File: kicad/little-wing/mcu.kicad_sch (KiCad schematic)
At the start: 31 parts, among them SW2 Reset, U1 ${ALTIUM_VALUE}, X1 ${ALTIUM_VALUE}, X2 ${ALTIUM_VALUE}

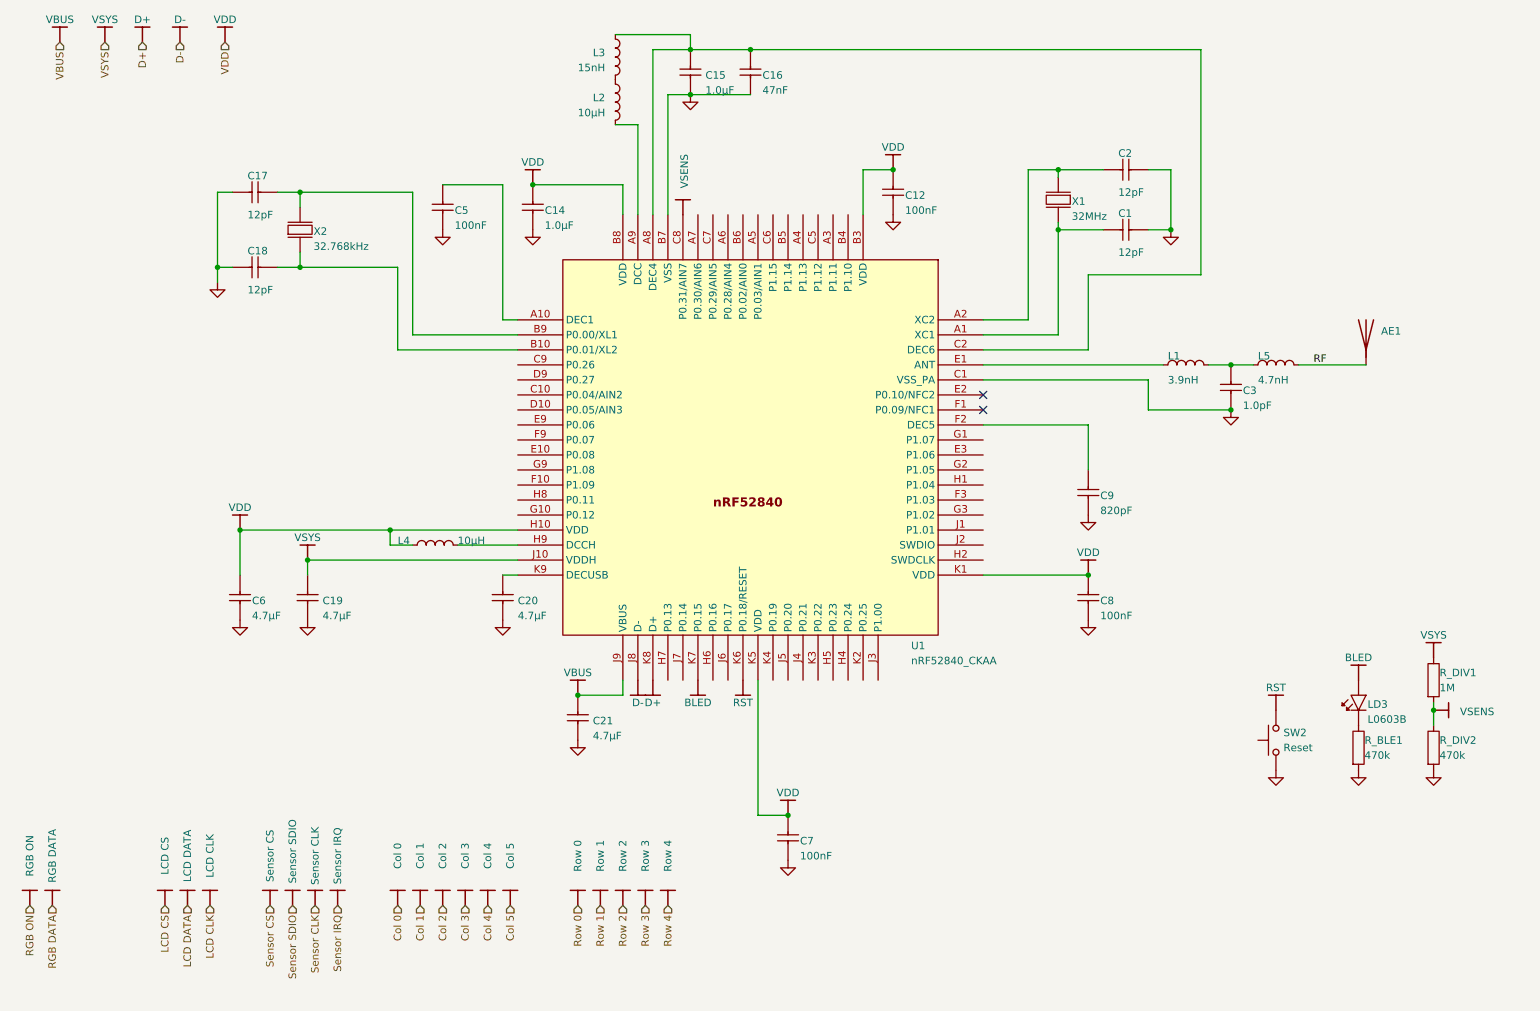
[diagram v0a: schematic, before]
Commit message: Reseting all the extra components sizes
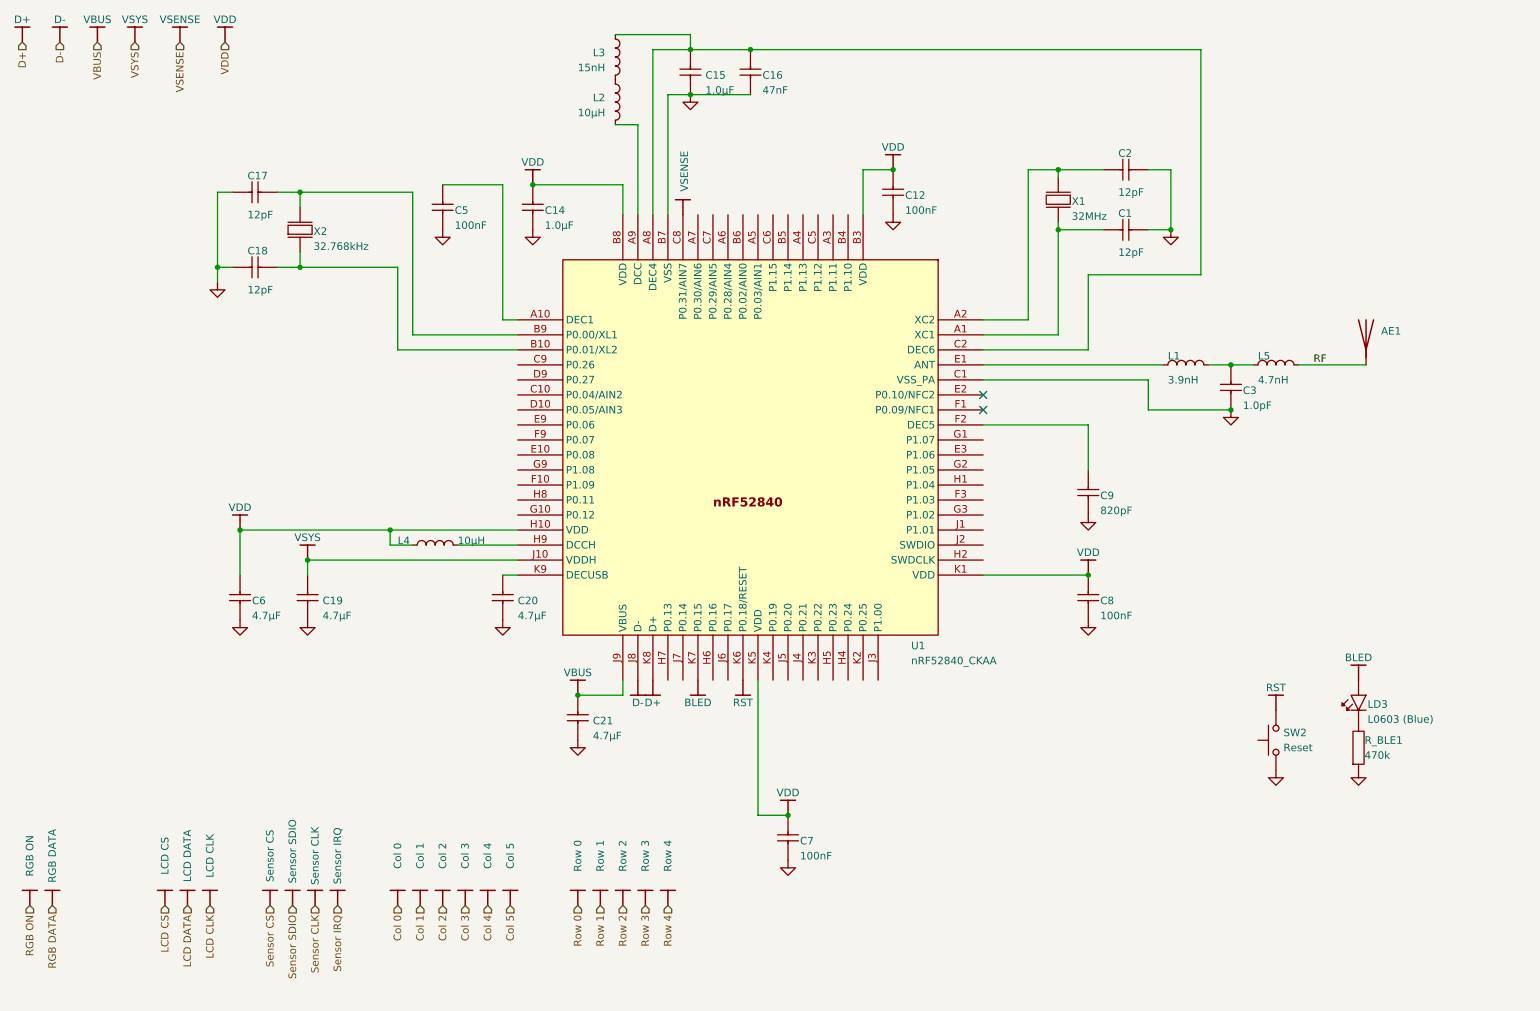
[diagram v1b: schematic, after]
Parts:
- removed R_DIV1: 1M, RESC0603X03L_C, symbol AltiumLib:root_3_mirrored_RES_AltiumLib.DbLib
- removed R_DIV2: 470k, RESC0603X03L_C, symbol AltiumLib:root_3_mirrored_RES_AltiumLib.DbLib
- LD3: value L0603B -> L0603 (Blue); footprint LED_0603_R -> LED_SMD:LED_0201_0603Metric
- R_BLE1: footprint RESC0603X03L_C -> Resistor_SMD:R_0201_0603Metric
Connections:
- net VSENS renamed VSENSE

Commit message: Swapping the crystals for smaller ones
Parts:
- X1: footprint BT-XTAL_2016 -> Crystal:Crystal_SMD_1210-4Pin_1.2x1.0mm
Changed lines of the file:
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@@
 			)
 		)
-		(property "Footprint" "BT-XTAL_2016"
+		(property "Footprint" "Crystal:Crystal_SMD_1210-4Pin_1.2x1.0mm"
 			(at 198.12 57.15 0)
 			(effects

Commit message: Dialing in the physical package
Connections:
- no-connect marks 2 -> 5
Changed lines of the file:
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@@
+	)
+	(no_connect
+		(at 154.94 55.88)
+	)
+	(no_connect
+		(at 160.02 55.88)
 	)
 	(no_connect
@@
 		(at 185.42 88.9)
 	)
+	(no_connect
+		(at 147.32 55.88)
+	)
 	(wire

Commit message: Backporting footprints from the PCB back to schematic
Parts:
- AE1: footprint JTI Antenna:ANTC3216X140N -> YAGEO Antenna:ANT2012LL13R2400A
- C1, C17, C18, C2, C3, C5, C7, C8, C9: footprint CAPC0603X03L_C -> Capacitor_SMD:C_0201_0603Metric
- C12, C16: footprint CAPC0603X03L_C -> Passive:CAPC0603X03L_C
- C14, C15, C19, C20, C21, C6: footprint CAPC1608X06L -> Passive:CAPC1608X06L
- L1: footprint INDC0603X03L_C -> Inductors$:INDC0603X03L_C
- L2: footprint INDC1608X06L -> 0603:INDC1608X06L
- L3: footprint INDC1005X04L -> 0402:INDC1005X04L
- L4: footprint INDC1608X06L -> Passive:INDC1608X06L
- L5: footprint INDC0603X03L_C -> Passive:INDC0603X03L_C
- SW2: footprint Button_Switch_SMD:SW_SPST_B3U-1000P -> Button_Switch_SMD:SW_SPST_B3U-3000P
- U1: footprint BGA94C35P10X10_352X356X50 -> nRF Devices$:BGA94C35P10X10_352X356X50
- X2: footprint XTAL_2012 -> EXC-1210:XTAL_ECS32761210TR
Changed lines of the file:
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@@
 			)
 		)
-		(property "Footprint" "BGA94C35P10X10_352X356X50"
+		(property "Footprint" "nRF Devices$:BGA94C35P10X10_352X356X50"
 			(at 114.3 127 0)
 			(effects
@@
 			)
 		)
-		(property "Footprint" "CAPC0603X03L_C"
+		(property "Footprint" "Capacitor_SMD:C_0201_0603Metric"
 			(at 205.74 58.42 0)
 			(effects
@@
 			)
 		)
-		(property "Footprint" "CAPC1608X06L"
+		(property "Footprint" "Passive:CAPC1608X06L"
 			(at 135.89 35.56 0)
 			(effects
@@
 			)
 		)
-		(property "Footprint" "Button_Switch_SMD:SW_SPST_B3U-1000P"
+		(property "Footprint" "Button_Switch_SMD:SW_SPST_B3U-3000P"
 			(at 229.87 144.78 0)
 			(effects
@@
 			)
 		)
-		(property "Footprint" "CAPC0603X03L_C"
+		(property "Footprint" "Passive:CAPC0603X03L_C"
 			(at 146.05 27.94 0)
 			(effects
@@
 			)
 		)
-		(property "Footprint" "CAPC0603X03L_C"
+		(property "Footprint" "Capacitor_SMD:C_0201_0603Metric"
 			(at 227.33 88.9 0)
 			(effects
@@
 			)
 		)
-		(property "Footprint" "INDC1608X06L"
+		(property "Footprint" "Passive:INDC1608X06L"
 			(at 88.9 111.76 0)
 			(effects
@@
 			)
 		)
-		(property "Footprint" "CAPC1608X06L"
+		(property "Footprint" "Passive:CAPC1608X06L"
 			(at 104.14 116.84 0)
 			(effects
@@
 			)
 		)
-		(property "Footprint" "CAPC0603X03L_C"
+		(property "Footprint" "Capacitor_SMD:C_0201_0603Metric"
 			(at 205.74 48.26 0)
 			(effects
@@
 			)
 		)
-		(property "Footprint" "INDC0603X03L_C"
+		(property "Footprint" "Passive:INDC0603X03L_C"
 			(at 231.14 81.28 0)
 			(effects
@@
 			)
 		)
-		(property "Footprint" "CAPC0603X03L_C"
+		(property "Footprint" "Capacitor_SMD:C_0201_0603Metric"
 			(at 66.04 52.07 0)
 			(effects
@@
 			)
 		)
-		(property "Footprint" "CAPC0603X03L_C"
+		(property "Footprint" "Capacitor_SMD:C_0201_0603Metric"
 			(at 152.4 157.48 0)
 			(effects
@@
 			)
 		)
-		(property "Footprint" "CAPC1608X06L"
+		(property "Footprint" "Passive:CAPC1608X06L"
 			(at 59.69 116.84 0)
 			(effects
@@
 			)
 		)
-		(property "Footprint" "CAPC0603X03L_C"
+		(property "Footprint" "Passive:CAPC0603X03L_C"
 			(at 170.18 48.26 0)
 			(effects
@@
 			)
 		)
-		(property "Footprint" "CAPC1608X06L"
+		(property "Footprint" "Passive:CAPC1608X06L"
 			(at 109.22 50.8 0)
 			(effects
@@
 			)
 		)
-		(property "Footprint" "CAPC0603X03L_C"
+		(property "Footprint" "Capacitor_SMD:C_0201_0603Metric"
 			(at 203.2 116.84 0)
 			(effects
@@
 			)
 		)
-		(property "Footprint" "JTI Antenna:ANTC3216X140N"
+		(property "Footprint" "YAGEO Antenna:ANT2012LL13R2400A"
 			(at 250.19 76.2 0)
 			(effects
@@
 			)
 		)
-		(property "Footprint" "INDC1005X04L"
+		(property "Footprint" "0402:INDC1005X04L"
 			(at 123.19 25.4 0)
 			(effects
@@
 			)
 		)
-		(property "Footprint" "CAPC1608X06L"
+		(property "Footprint" "Passive:CAPC1608X06L"
 			(at 71.12 116.84 0)
 			(effects
@@
 			)
 		)
-		(property "Footprint" "CAPC0603X03L_C"
+		(property "Footprint" "Capacitor_SMD:C_0201_0603Metric"
 			(at 66.04 64.77 0)
 			(effects
@@
 			)
 		)
-		(property "Footprint" "CAPC0603X03L_C"
+		(property "Footprint" "Capacitor_SMD:C_0201_0603Metric"
 			(at 203.2 99.06 0)
 			(effects
@@
 			)
 		)
-		(property "Footprint" "CAPC1608X06L"
+		(property "Footprint" "Passive:CAPC1608X06L"
 			(at 116.84 137.16 0)
 			(effects
@@
 			)
 		)
-		(property "Footprint" "CAPC0603X03L_C"
+		(property "Footprint" "Capacitor_SMD:C_0201_0603Metric"
 			(at 93.98 50.8 0)
 			(effects
@@
 			)
 		)
-		(property "Footprint" "INDC0603X03L_C"
+		(property "Footprint" "Inductors$:INDC0603X03L_C"
 			(at 215.9 81.28 0)
 			(effects
@@
 			)
 		)
-		(property "Footprint" "INDC1608X06L"
+		(property "Footprint" "0603:INDC1608X06L"
 			(at 123.19 33.02 0)
 			(effects
@@
 			)
 		)
-		(property "Footprint" "XTAL_2012"
+		(property "Footprint" "EXC-1210:XTAL_ECS32761210TR"
 			(at 69.85 54.61 0)
 			(effects

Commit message: Fixes and space optimisations
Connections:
- net BLED: now also U1.G10 (P0.12); no longer U1.K7 (P0.15)
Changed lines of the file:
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@@
 	)
 	(symbol
-		(lib_id "nrf52840_ckaa_var4-altium-import:VDD_nRF_BAR")
-		(at 137.16 134.62 0)
-		(unit 1)
-		(exclude_from_sim no)
-		(in_bom yes)
-		(on_board yes)
-		(dnp no)
-		(property "Reference" "#PWR0109"
-			(at 137.16 134.62 0)
-			(effects
-				(font
-					(size 1.27 1.27)
-				)
-				(hide yes)
-			)
-		)
-		(property "Value" "BLED"
-			(at 137.16 138.43 0)
-			(effects
-				(font
-					(size 1.27 1.27)
-				)
-			)
-		)
-		(property "Footprint" ""
-			(at 137.16 134.62 0)
-			(effects
-				(font
-					(size 1.27 1.27)
-				)
-			)
-		)
-		(property "Datasheet" ""
-			(at 137.16 134.62 0)
-			(effects
-				(font
-					(size 1.27 1.27)
-				)
-			)
-		)
-		(property "Description" ""
-			(at 137.16 134.62 0)
-			(effects
-				(font
-					(size 1.27 1.27)
-				)
-			)
-		)
-		(pin ""
-		)
-		(instances
-			(project "little-wing"
-				(path "/3a835e6f-a660-4b38-a102-87841cdd95ed/eaaf4618-ba3d-41b4-8a99-4f719e243661/ebcf195d-f1fd-431a-a78e-86a1a85cb647"
-					(reference "#PWR0109")
-					(unit 1)
-				)
-			)
-		)
-	)
-	(symbol
 		(lib_id "npm1100_caax_config1-altium-import:VBUS_BAR")
 		(at 90.17 172.72 180)
@@
 					(unit 1)
 				)
+			)
+		)
+	)
+	(symbol
+		(lib_id "nrf52840_ckaa_var4-altium-import:VDD_nRF_BAR")
+		(at 106.68 106.68 270)
+		(unit 1)
+		(exclude_from_sim no)
+		(in_bom yes)
+		(on_board yes)
+		(dnp no)
+		(property "Reference" "#PWR064"
+			(at 106.68 106.68 0)
+			(effects
+				(font
+					(size 1.27 1.27)
+				)
+				(hide yes)
+			)
+		)
+		(property "Value" "BLED"
+			(at 102.87 106.68 0)
+			(effects
+				(font
+					(size 1.27 1.27)
+				)
+			)
+		)
+		(property "Footprint" ""
+			(at 106.68 106.68 0)
+			(effects
+				(font
+					(size 1.27 1.27)
+				)
+			)
+		)
+		(property "Datasheet" ""
+			(at 106.68 106.68 0)
+			(effects
+				(font
+					(size 1.27 1.27)
+				)
+			)
+		)
+		(property "Description" ""
+			(at 106.68 106.68 0)
+			(effects
+				(font
+					(size 1.27 1.27)
+				)
+			)
+		)
+		(pin ""
+		)
+		(instances
+			(project "little-wing"
+				(path "/3a835e6f-a660-4b38-a102-87841cdd95ed/eaaf4618-ba3d-41b4-8a99-4f719e243661/ebcf195d-f1fd-431a-a78e-86a1a85cb647"
+					(reference "#PWR064")
+					(unit 1)
+				)

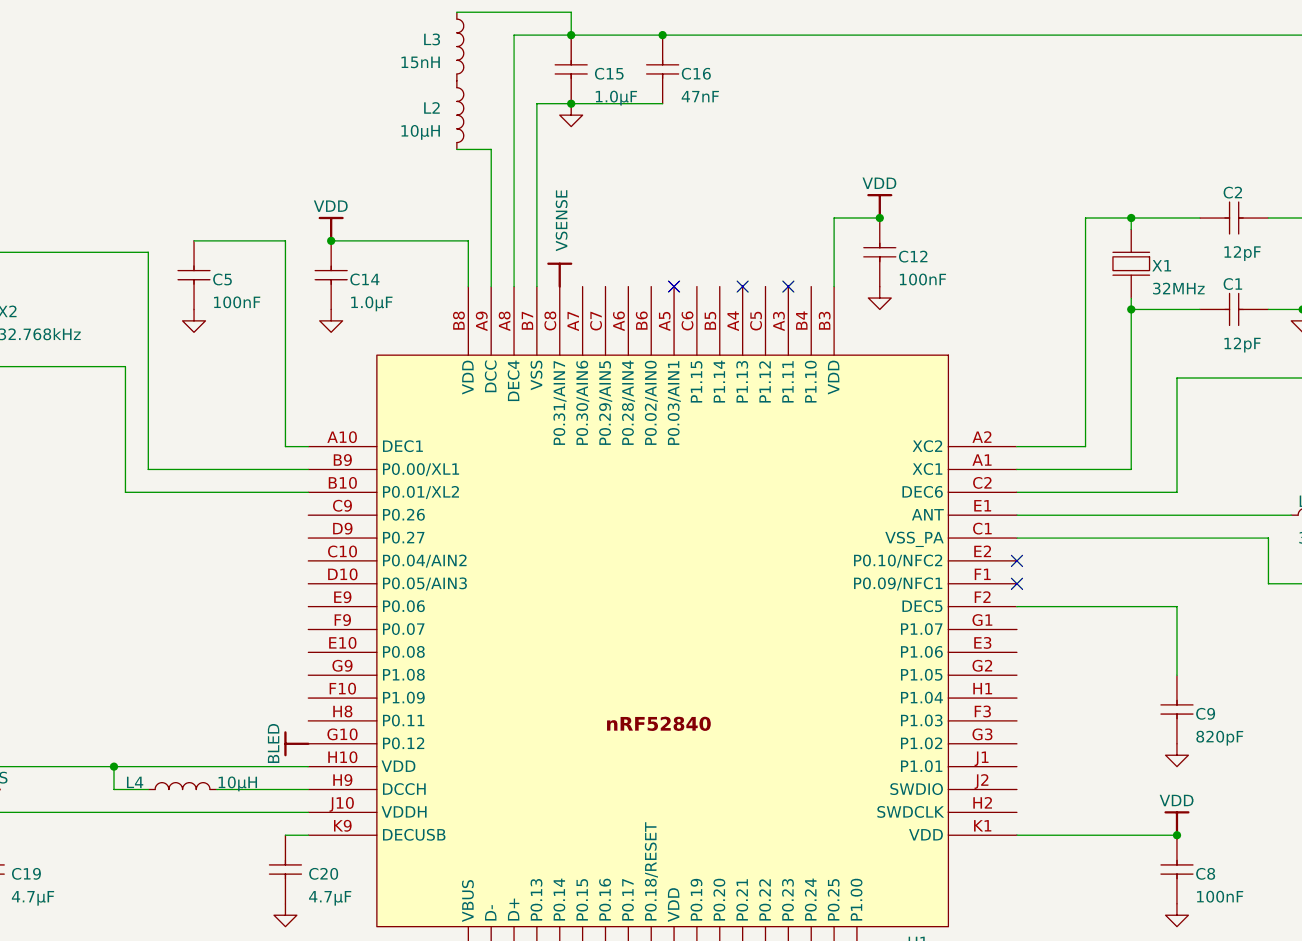
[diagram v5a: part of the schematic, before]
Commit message: Loosely attaching pins to prefiery
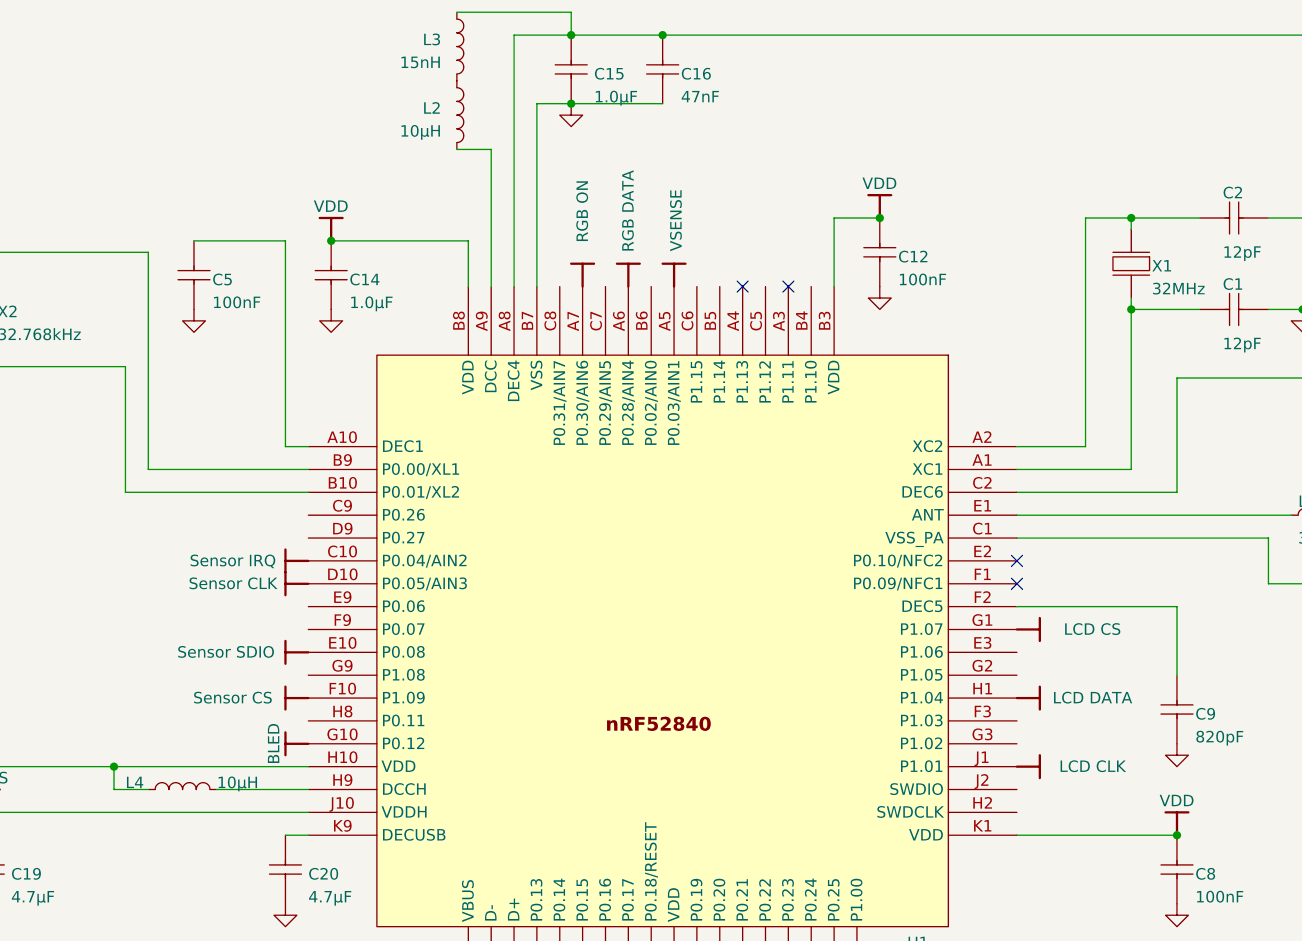
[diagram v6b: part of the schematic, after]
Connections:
- net LCD CLK: now also U1.J1 (P1.01)
- net LCD CS: now also U1.G1 (P1.07)
- net LCD DATA: now also U1.H1 (P1.04)
- net RGB DATA: now also U1.A6 (P0.28/AIN4)
- net RGB ON: now also U1.A7 (P0.30/AIN6)
- net Sensor CLK: now also U1.D10 (P0.05/AIN3)
- net Sensor CS: now also U1.F10 (P1.09)
- net Sensor IRQ: now also U1.C10 (P0.04/AIN2)
- net Sensor SDIO: now also U1.E10 (P0.08)
- net VSENSE: now also U1.A5 (P0.03/AIN1); no longer U1.C8 (P0.31/AIN7)
- no-connect marks 5 -> 4
